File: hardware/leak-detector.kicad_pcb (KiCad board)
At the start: 2 copper layers, 23.5 x 27.5 mm, 21 parts, among them J1 Conn_Atmel_ISP_TagConnect_TC2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, SW1 PTS810, U1 BMP581, U2 ATtiny25V

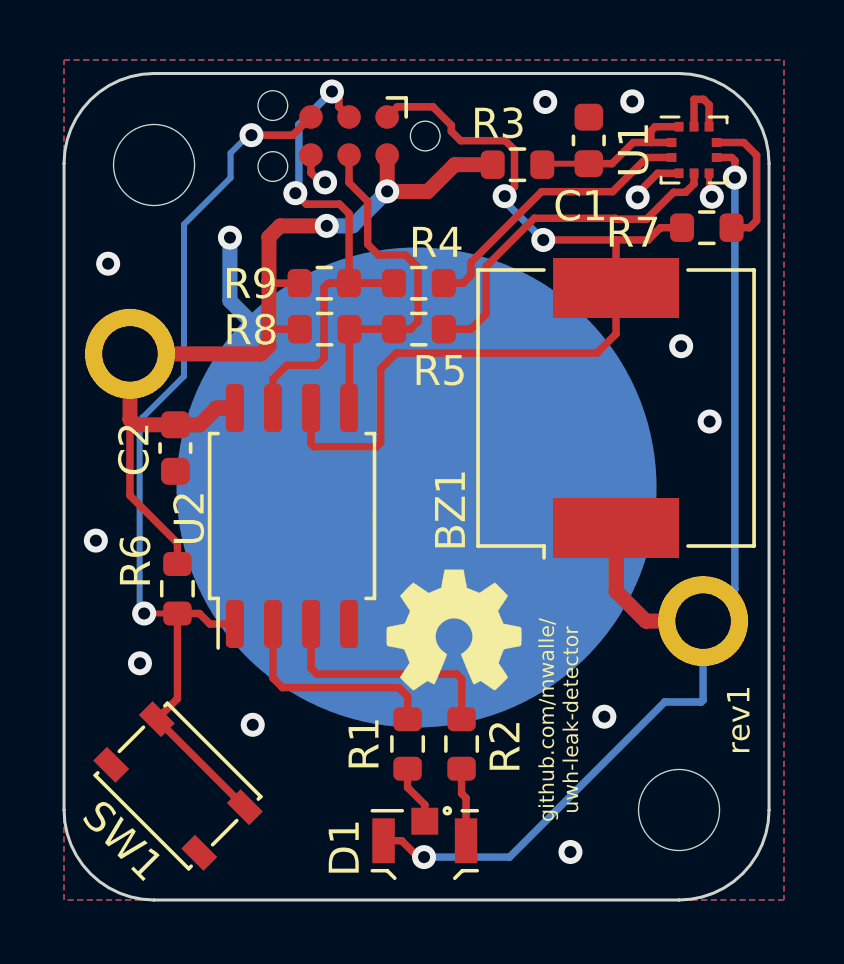
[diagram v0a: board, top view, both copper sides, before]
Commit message: hardware: update to attiny412
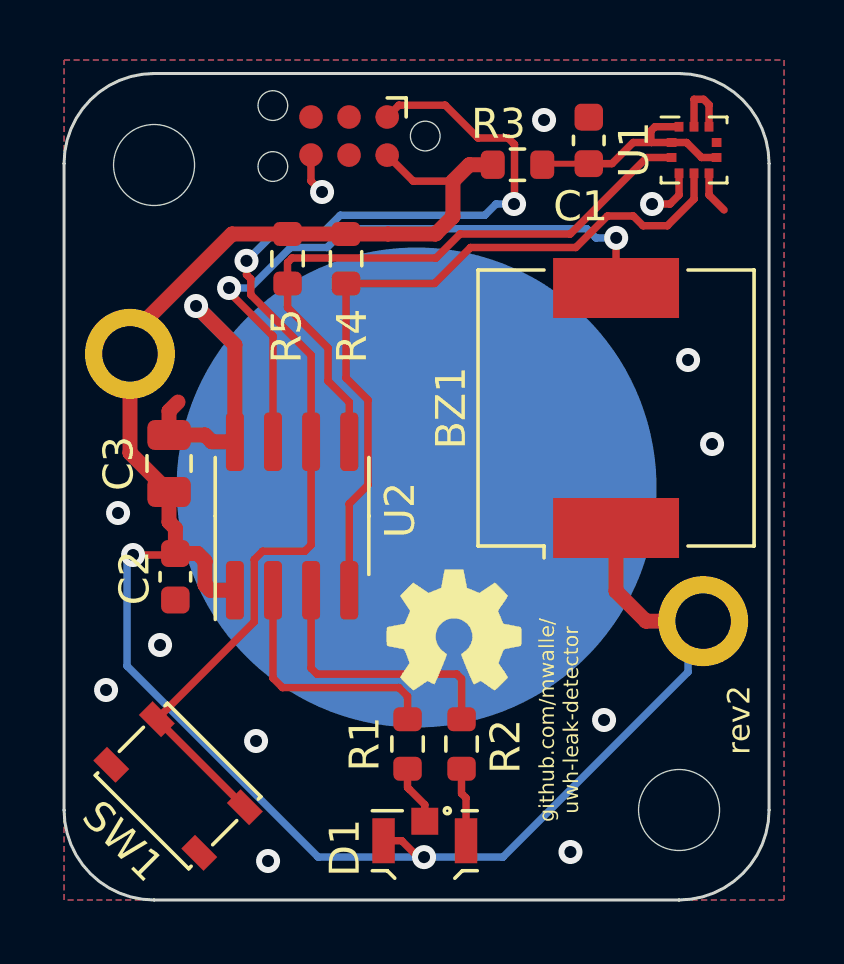
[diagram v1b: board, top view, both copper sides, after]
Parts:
- removed the R4 at (111.8, 69.4)
- removed the R5 at (111.8, 71.0)
- removed R6: 10k, Resistor_SMD:R_0603_1608Metric
- removed R7: 1k, Resistor_SMD:R_0603_1608Metric
- added C3: 10u, Capacitor_SMD:C_0805_2012Metric, F.Cu at (103.5, 75.5)
- BT1: value Battery_Cell -> CR2032
- R1: value 33R -> 100R
- R2: value 1k -> 560R
- U1: value BMP581 -> LPS22HH
- U2: value ATtiny25V -> ATtiny412; footprint Package_SO:SOIC-8_5.275x5.275mm_P1.27mm -> Package_SO:SOIC-8_3.9x4.9mm_P1.27mm
- moved C2 4.29 mm to (103.7, 79.2)
- moved R4 2.45 mm to (109.4, 68.6), turned to -90 degrees
- moved R5 1.47 mm to (107.5, 68.6), turned to -90 degrees
- renumbered R8 to R4, R9 to R5
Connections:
- net Net-(R1-Pad2) renamed /LED_RED
- net Net-(R2-Pad2) renamed /LED_GREEN
- J1 pad 1: /BUZZER -> /~{RST}/UPDI
- J1 pad 3: /SCL -> unconnected-(J1-Pad3)
- J1 pad 4: /SDA -> unconnected-(J1-Pad4)
- J1 pad 5: /~{RST} -> unconnected-(J1-Pad5)
- SW1 pad 2: /~{RST} -> /~{RST}/UPDI
- U1 pad 2: Net-(R4-Pad1) -> /SCL
- U1 pad 4: Net-(R5-Pad1) -> /SDA
- U1 pad 6: VCC -> Net-(C1-Pad1)
- U1 pad 7: Net-(R7-Pad1) -> unconnected-(U1-Pad7)
- U2 pad 1: /~{RST} -> VCC
- U2 pad 4: GND -> /SDA
- U2 pad 5: /SDA -> /SCL
- U2 pad 6: /BUZZER -> /~{RST}/UPDI
- U2 pad 7: /SCL -> /BUZZER
- U2 pad 8: VCC -> GND
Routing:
- net /~{RST}/UPDI: track 0.00 -> 39.9 mm, vias 0 -> 2
- net /~{RST}: track 31.0 -> 0.00 mm, vias 2 -> 0
- net /SDA: track 12.0 -> 24.7 mm
- net Net-(R5-Pad1): track 11.7 -> 0.00 mm
- net /BUZZER: track 31.1 -> 21.3 mm
- net Net-(R4-Pad1): track 9.59 -> 0.00 mm
- net GND: track 16.9 -> 25.2 mm, vias 14 -> 13
- net Net-(R7-Pad1): track 4.62 -> 0.00 mm
- net /SCL: track 17.1 -> 21.1 mm, vias 2 -> 0
- net VCC: track 69.1 -> 66.6 mm, vias 4 -> 2
- net Net-(C1-Pad1): track 6.01 -> 7.72 mm
- net /LED_RED: track 7.26 -> 8.43 mm
- net /LED_GREEN: track 7.93 -> 9.11 mm
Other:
- board text added: "rev2"
- board text removed: "rev1"
